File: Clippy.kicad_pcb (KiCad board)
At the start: 2 copper layers, 61.2 x 38.4 mm, 19 parts, among them J1 Conn_01x08, SW1 PEC12R-4215F-S0024, U1 tiny2040, U2 SN74LV1T34DBV

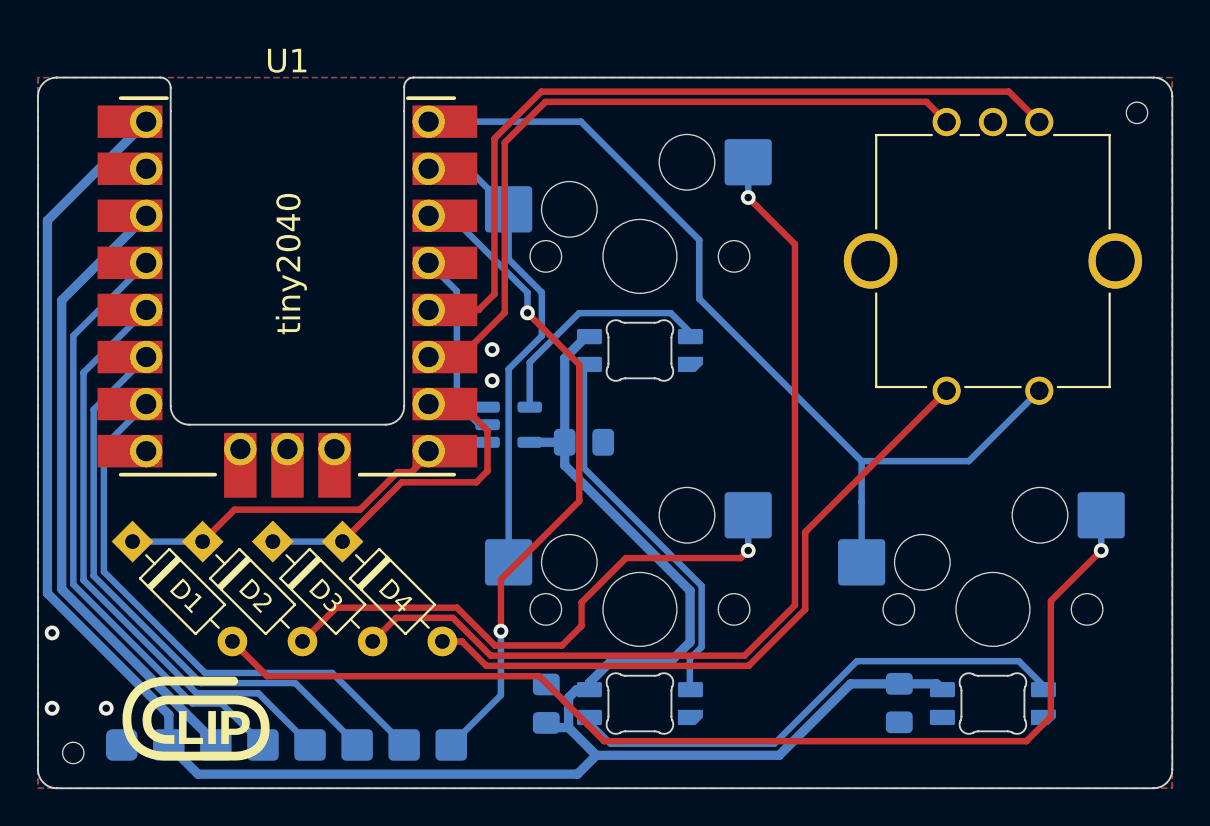
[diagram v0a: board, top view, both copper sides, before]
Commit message: RP2040-Zero compatibility
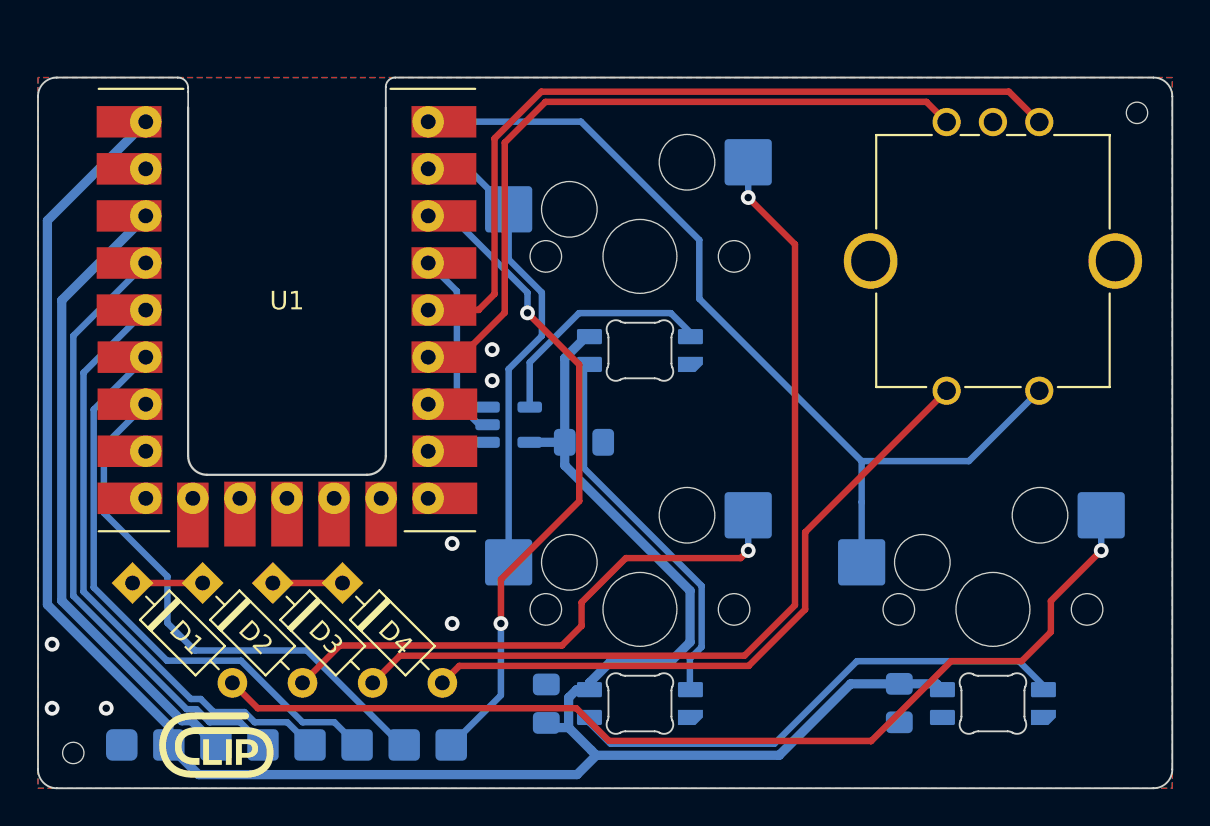
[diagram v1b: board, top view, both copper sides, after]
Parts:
- U1: value tiny2040 -> RP2040-Zero; footprint tiny2040:tiny2040 -> RP2040-Zero:RP2040 Zero
- moved U1 15.4 mm to (125.7, 84.0)
- moved D1 2.24 mm to (127.5, 86.0)
- moved D2 2.24 mm to (131.3, 86.0)
- moved D3 2.24 mm to (135.1, 86.0)
- moved D4 2.24 mm to (138.9, 86.0)
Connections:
- SW1 pad A: ENC0 -> ENCA
- SW1 pad B: ENC1 -> ENCB
- U1 pad 10: ROW0 -> COL1
- U1 pad 11: ENC1 -> COL0
- U1 pad 12: ENC0 -> GP2
- U1 pad 14: GP2 -> ENCA
- U1 pad 15: COL0 -> ENCB
- U1 pad 16: COL1 -> GP10
- U1 pad 17: unconnected-(U1-CLK-Pad17) -> GP11
- U1 pad 18: GND -> GP8
- U1 pad 19: unconnected-(U1-DIO-Pad19) -> GP13
- U1 pad 8: GND -> GP15
- U1 pad 9: ROW1 -> GP14
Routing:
- net ENCA: track 0.00 -> 43.4 mm
- net ENC0: track 43.4 -> 0.00 mm
- net ENCB: track 0.00 -> 39.5 mm
- net ENC1: track 39.5 -> 0.00 mm
- net ROW0: track 19.1 -> 3.76 mm
- net ROW1: track 18.1 -> 3.78 mm
- net Net-(D1-A): track 58.9 -> 55.3 mm
- net Net-(D2-A): track 30.4 -> 29.7 mm
- net Net-(D3-A): track 50.2 -> 49.5 mm
- net GND: vias 5 -> 7
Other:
- outline, holes or cut-outs redrawn
